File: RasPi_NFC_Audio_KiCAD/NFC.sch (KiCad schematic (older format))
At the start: 33 parts

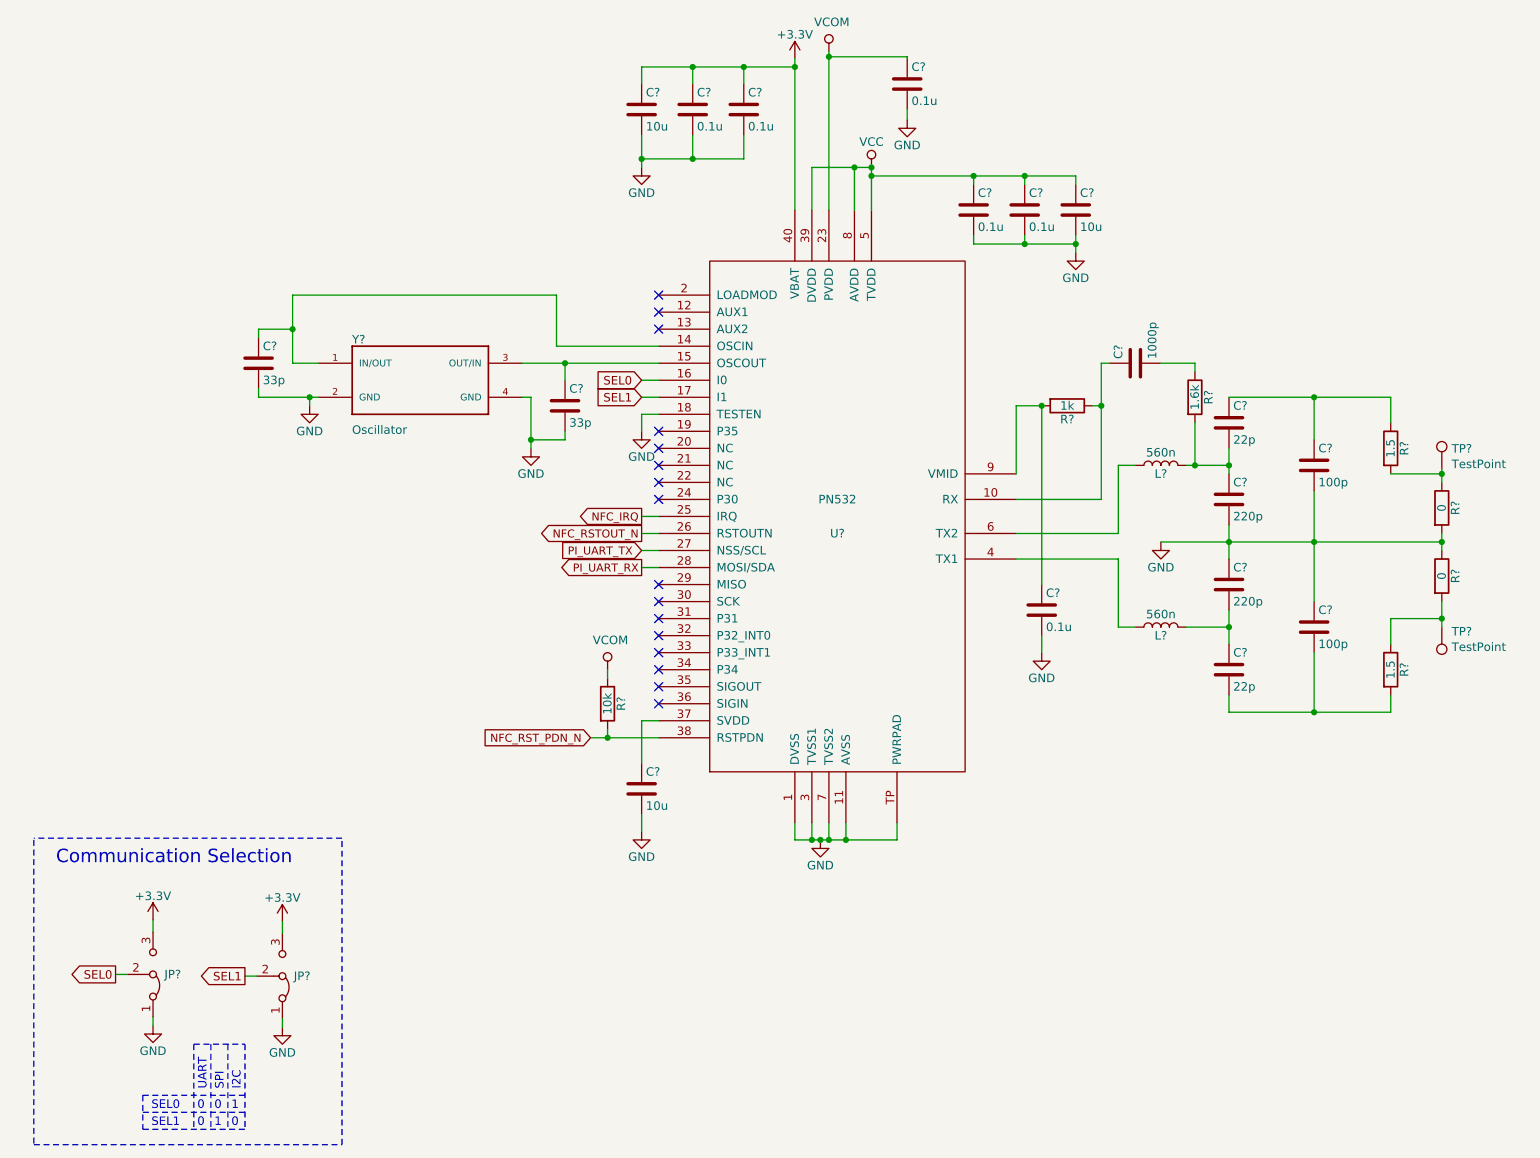
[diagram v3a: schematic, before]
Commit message: Schematic Updates
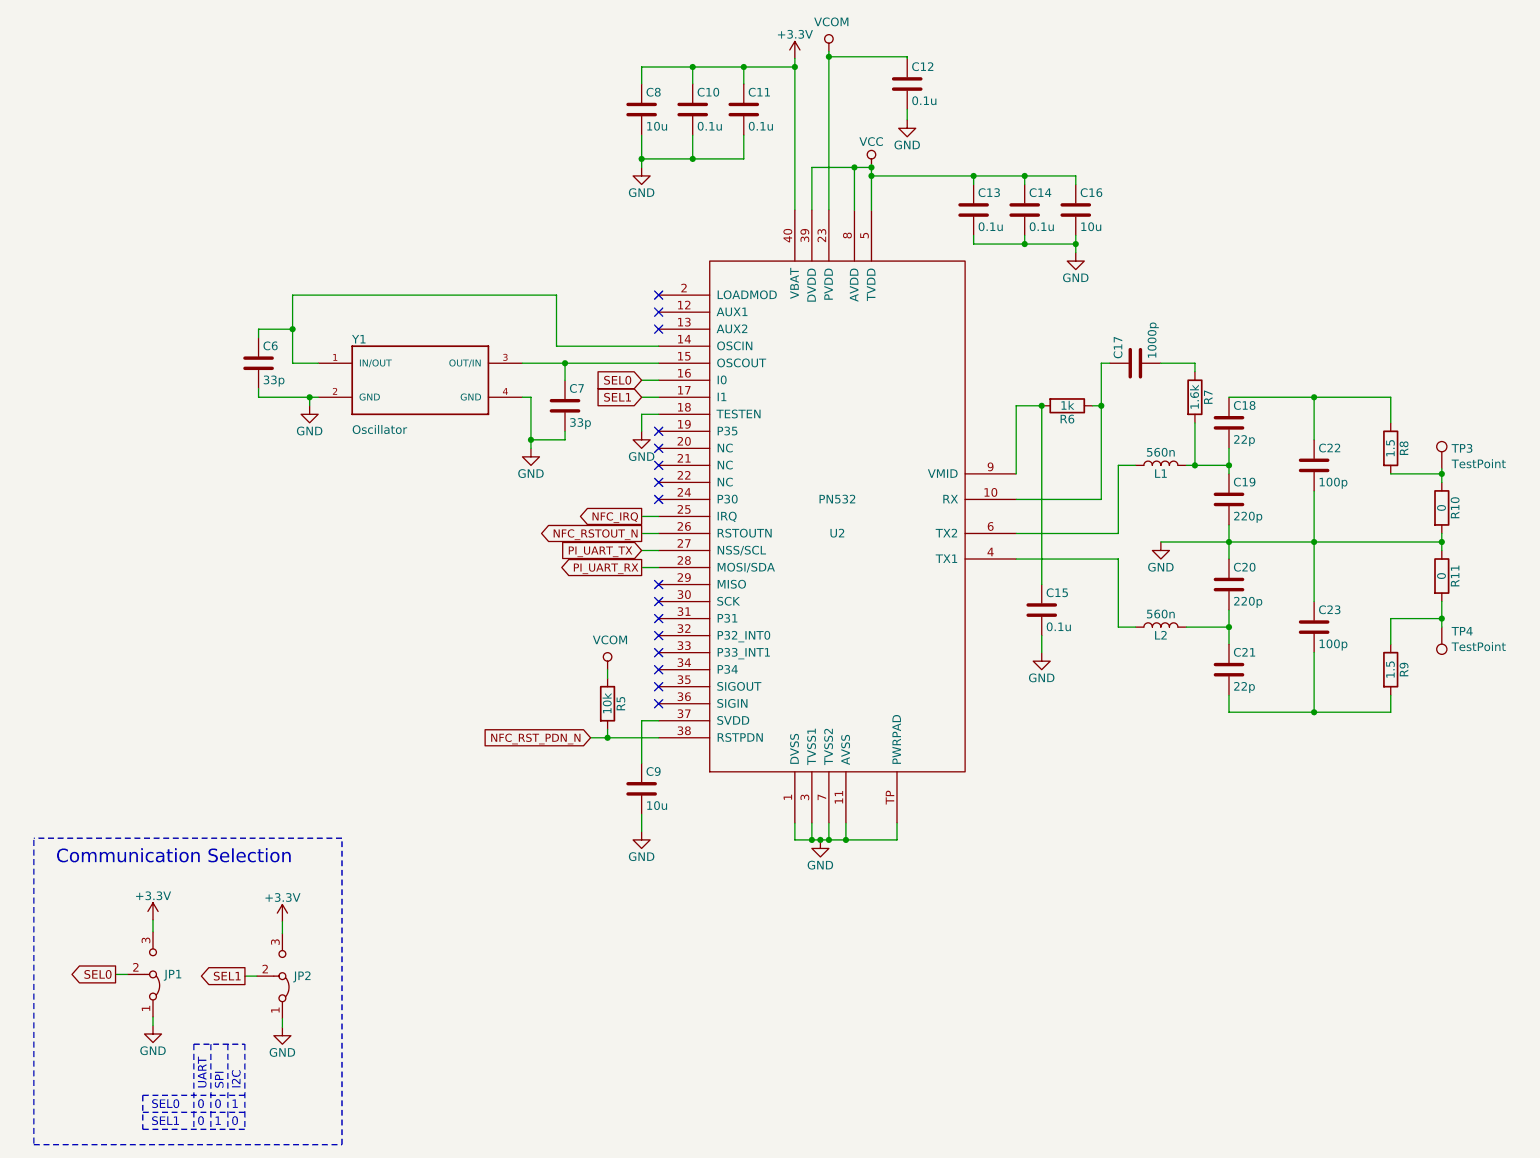
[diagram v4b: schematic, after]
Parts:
- gave numbers to parts that had none: 33
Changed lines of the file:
@@
 $EndDescr
 $Comp
-L PN532:PN532 U?
+L PN532:PN532 U2
 U 1 1 5ACE3C9F
 P 6400 3740
-F 0 "U?" H 6400 3640 50  0000 C CNN
+F 0 "U2" H 6400 3640 50  0000 C CNN
 F 1 "PN532" H 6400 3840 50  0000 C CNN
 F 2 "NFC_Toy_Lib:HVQFN40-6X6" H 6400 3740 50  0001 C CNN
@@
 	5250 4040 5350 4040
 $Comp
-L Oscillator:Oscillator Y?
+L Oscillator:Oscillator Y1
 U 1 1 5ACE46F9
 P 3950 2940
-F 0 "Y?" H 3549 3150 50  0000 L BNN
+F 0 "Y1" H 3549 3150 50  0000 L BNN
 F 1 "Oscillator" H 3549 2619 50  0000 L BNN
 F 2 "NFC_Toy_Lib:OSCCC500X320X105N" H 3950 2940 50  0001 L BNN
@@
 	6250 1690 6500 1690
 $Comp
-L Device:L L?
+L Device:L L1
 U 1 1 5ACEADE9
 P 8300 3440
-F 0 "L?" V 8250 3440 50  0000 C CNN
+F 0 "L1" V 8250 3440 50  0000 C CNN
 F 1 "560n" V 8375 3440 50  0000 C CNN
 F 2 "Inductors_SMD:L_0603_HandSoldering" H 8300 3440 50  0001 C CNN
@@
 $EndComp
 $Comp
-L Device:C C?
+L Device:C C19
 U 1 1 5ACEAE3A
 P 8700 3640
-F 0 "C?" H 8725 3740 50  0000 L CNN
+F 0 "C19" H 8725 3740 50  0000 L CNN
 F 1 "220p" H 8725 3540 50  0000 L CNN
 F 2 "Capacitors_SMD:C_0402" H 8738 3490 50  0001 C CNN
@@
 Connection ~ 6500 1690
 $Comp
-L Device:L L?
+L Device:L L2
 U 1 1 5ACEB747
 P 8300 4390
-F 0 "L?" V 8250 4390 50  0000 C CNN
+F 0 "L2" V 8250 4390 50  0000 C CNN
 F 1 "560n" V 8375 4390 50  0000 C CNN
 F 2 "Inductors_SMD:L_0603_HandSoldering" H 8300 4390 50  0001 C CNN
@@
 $EndComp
 $Comp
-L Device:C C?
+L Device:C C20
 U 1 1 5ACEB85B
 P 8700 4140
-F 0 "C?" H 8725 4240 50  0000 L CNN
+F 0 "C20" H 8725 4240 50  0000 L CNN
 F 1 "220p" H 8725 4040 50  0000 L CNN
 F 2 "Capacitors_SMD:C_0402" H 8738 3990 50  0001 C CNN
@@
 	8700 3340 8700 3440
 $Comp
-L Device:C C?
+L Device:C C18
 U 1 1 5ACEB929
 P 8700 3190
-F 0 "C?" H 8725 3290 50  0000 L CNN
+F 0 "C18" H 8725 3290 50  0000 L CNN
 F 1 "22p" H 8725 3090 50  0000 L CNN
 F 2 "Capacitors_SMD:C_0402" H 8738 3040 50  0001 C CNN
@@
 $EndComp
 $Comp
-L Device:C C?
+L Device:C C21
 U 1 1 5ACEB967
 P 8700 4640
-F 0 "C?" H 8725 4740 50  0000 L CNN
+F 0 "C21" H 8725 4740 50  0000 L CNN
 F 1 "22p" H 8725 4540 50  0000 L CNN
 F 2 "Capacitors_SMD:C_0402" H 8738 4490 50  0001 C CNN
@@
 $EndComp
 $Comp
-L Device:C C?
+L Device:C C23
 U 1 1 5ACEB9A1
 P 9200 4390
-F 0 "C?" H 9225 4490 50  0000 L CNN
+F 0 "C23" H 9225 4490 50  0000 L CNN
 F 1 "100p" H 9225 4290 50  0000 L CNN
 F 2 "Capacitors_SMD:C_0402" H 9238 4240 50  0001 C CNN
@@
 $EndComp
 $Comp
-L Device:C C?
+L Device:C C22
 U 1 1 5ACEB9F3
 P 9200 3440
-F 0 "C?" H 9225 3540 50  0000 L CNN
+F 0 "C22" H 9225 3540 50  0000 L CNN
 F 1 "100p" H 9225 3340 50  0000 L CNN
 F 2 "Capacitors_SMD:C_0402" H 9238 3290 50  0001 C CNN
@@
 Connection ~ 9200 3890
 $Comp
-L Device:R R?
+L Device:R R9
 U 1 1 5ACEBF6E
 P 9650 4640
-F 0 "R?" V 9730 4640 50  0000 C CNN
+F 0 "R9" V 9730 4640 50  0000 C CNN
 F 1 "1.5" V 9650 4640 50  0000 C CNN
 F 2 "Resistors_SMD:R_0603_HandSoldering" V 9580 4640 50  0001 C CNN
@@
 $EndComp
 $Comp
-L Device:R R?
+L Device:R R8
 U 1 1 5ACEBF75
 P 9650 3340
-F 0 "R?" V 9730 3340 50  0000 C CNN
+F 0 "R8" V 9730 3340 50  0000 C CNN
 F 1 "1.5" V 9650 3340 50  0000 C CNN
 F 2 "Resistors_SMD:R_0603_HandSoldering" V 9580 3340 50  0001 C CNN
@@
 Connection ~ 9200 3040
 $Comp
-L Device:R R?
+L Device:R R10
 U 1 1 5ACEC09A
 P 9950 3690
-F 0 "R?" V 10030 3690 50  0000 C CNN
+F 0 "R10" V 10030 3690 50  0000 C CNN
 F 1 "0" V 9950 3690 50  0000 C CNN
 F 2 "Resistors_SMD:R_0402" V 9880 3690 50  0001 C CNN
@@
 $EndComp
 $Comp
-L Device:R R?
+L Device:R R11
 U 1 1 5ACEC0EF
 P 9950 4090
-F 0 "R?" V 10030 4090 50  0000 C CNN
+F 0 "R11" V 10030 4090 50  0000 C CNN
 F 1 "0" V 9950 4090 50  0000 C CNN
 F 2 "Resistors_SMD:R_0402" V 9880 4090 50  0001 C CNN
@@
 	9950 4240 9950 4340
 $Comp
-L Device:R R?
+L Device:R R7
 U 1 1 5ACEC27D
 P 8500 3040
-F 0 "R?" V 8580 3040 50  0000 C CNN
+F 0 "R7" V 8580 3040 50  0000 C CNN
 F 1 "1.6k" V 8500 3040 50  0000 C CNN
 F 2 "Resistors_SMD:R_0603_HandSoldering" V 8430 3040 50  0001 C CNN
@@
 Connection ~ 8500 3440
 $Comp
-L Device:C C?
+L Device:C C17
 U 1 1 5ACEC388
 P 8150 2840
-F 0 "C?" H 8175 2940 50  0000 L CNN
+F 0 "C17" H 8175 2940 50  0000 L CNN
 F 1 "1000p" H 8175 2740 50  0000 L CNN
 F 2 "Capacitors_SMD:C_0402" H 8188 2690 50  0001 C CNN
@@
 	7950 3640 7450 3640
 $Comp
-L Device:R R?
+L Device:R R6
 U 1 1 5ACEC51A
 P 7750 3090
-F 0 "R?" V 7830 3090 50  0000 C CNN
+F 0 "R6" V 7830 3090 50  0000 C CNN
 F 1 "1k" V 7750 3090 50  0000 C CNN
 F 2 "Resistors_SMD:R_0603_HandSoldering" V 7680 3090 50  0001 C CNN
@@
 $EndComp
 $Comp
-L Device:C C?
+L Device:C C15
 U 1 1 5ACEC7D8
 P 7600 4290
-F 0 "C?" H 7625 4390 50  0000 L CNN
+F 0 "C15" H 7625 4390 50  0000 L CNN
 F 1 "0.1u" H 7625 4190 50  0000 L CNN
 F 2 "Capacitors_SMD:C_0402" H 7638 4140 50  0001 C CNN
@@
 	3000 3040 3300 3040
 $Comp
-L Device:C C?
+L Device:C C6
 U 1 1 5ACED3C6
 P 3000 2840
-F 0 "C?" H 3025 2940 50  0000 L CNN
+F 0 "C6" H 3025 2940 50  0000 L CNN
 F 1 "33p" H 3025 2740 50  0000 L CNN
 F 2 "Capacitors_SMD:C_0402" H 3038 2690 50  0001 C CNN
@@
 Connection ~ 3200 2640
 $Comp
-L Device:C C?
+L Device:C C7
 U 1 1 5ACED68A
 P 4800 3090
-F 0 "C?" H 4825 3190 50  0000 L CNN
+F 0 "C7" H 4825 3190 50  0000 L CNN
 F 1 "33p" H 4825 2990 50  0000 L CNN
 F 2 "Capacitors_SMD:C_0402" H 4838 2940 50  0001 C CNN
@@
 Connection ~ 6350 5640
 $Comp
-L Device:R R?
+L Device:R R5
 U 1 1 5ACEF2A4
 P 5050 4840
-F 0 "R?" V 5130 4840 50  0000 C CNN
+F 0 "R5" V 5130 4840 50  0000 C CNN
 F 1 "10k" V 5050 4840 50  0000 C CNN
 F 2 "Resistors_SMD:R_0603_HandSoldering" V 4980 4840 50  0001 C CNN
@@
 Connection ~ 5050 5040
 $Comp
-L Device:C C?
+L Device:C C13
 U 1 1 5ACEFF35
 P 7200 1940
-F 0 "C?" H 7225 2040 50  0000 L CNN
+F 0 "C13" H 7225 2040 50  0000 L CNN
 F 1 "0.1u" H 7225 1840 50  0000 L CNN
 F 2 "Capacitors_SMD:C_0402" H 7238 1790 50  0001 C CNN
@@
 $EndComp
 $Comp
-L Device:C C?
+L Device:C C14
 U 1 1 5ACEFFEF
 P 7500 1940
-F 0 "C?" H 7525 2040 50  0000 L CNN
+F 0 "C14" H 7525 2040 50  0000 L CNN
 F 1 "0.1u" H 7525 1840 50  0000 L CNN
 F 2 "Capacitors_SMD:C_0402" H 7538 1790 50  0001 C CNN
@@
 $EndComp
 $Comp
-L Device:C C?
+L Device:C C10
 U 1 1 5ACF004D
 P 5550 1350
-F 0 "C?" H 5575 1450 50  0000 L CNN
+F 0 "C10" H 5575 1450 50  0000 L CNN
 F 1 "0.1u" H 5575 1250 50  0000 L CNN
 F 2 "Capacitors_SMD:C_0402" H 5588 1200 50  0001 C CNN
@@
 $EndComp
 $Comp
-L Device:C C?
+L Device:C C11
 U 1 1 5ACF00B0
 P 5850 1350
-F 0 "C?" H 5875 1450 50  0000 L CNN
+F 0 "C11" H 5875 1450 50  0000 L CNN
 F 1 "0.1u" H 5875 1250 50  0000 L CNN
 F 2 "Capacitors_SMD:C_0402" H 5888 1200 50  0001 C CNN
@@
 	6600 1740 7200 1740
 $Comp
-L Device:C C?
+L Device:C C16
 U 1 1 5ACF059B
 P 7800 1940
-F 0 "C?" H 7825 2040 50  0000 L CNN
+F 0 "C16" H 7825 2040 50  0000 L CNN
 F 1 "10u" H 7825 1840 50  0000 L CNN
 F 2 "Capacitors_SMD:C_0603_HandSoldering" H 7838 1790 50  0001 C CNN
@@
 Connection ~ 5850 1100
 $Comp
-L Device:C C?
+L Device:C C8
 U 1 1 5ACF095C
 P 5250 1350
-F 0 "C?" H 5275 1450 50  0000 L CNN
+F 0 "C8" H 5275 1450 50  0000 L CNN
 F 1 "10u" H 5275 1250 50  0000 L CNN
 F 2 "Capacitors_SMD:C_0603_HandSoldering" H 5288 1200 50  0001 C CNN
@@
 Connection ~ 5550 1640
 $Comp
-L Device:C C?
+L Device:C C9
 U 1 1 5ACF126E
 P 5250 5340
-F 0 "C?" H 5275 5440 50  0000 L CNN
+F 0 "C9" H 5275 5440 50  0000 L CNN
 F 1 "10u" H 5275 5240 50  0000 L CNN
 F 2 "Capacitors_SMD:C_0603_HandSoldering" H 5288 5190 50  0001 C CNN
@@
 	6450 5640 6750 5640
 $Comp
-L Connector:TestPoint TP?
+L Connector:TestPoint TP3
 U 1 1 5E181FE8
 P 9950 3460
-F 0 "TP?" H 10008 3578 50  0000 L CNN
+F 0 "TP3" H 10008 3578 50  0000 L CNN
 F 1 "TestPoint" H 10008 3487 50  0000 L CNN
 F 2 "" H 10150 3460 50  0001 C CNN
@@
 $EndComp
 $Comp
-L Connector:TestPoint TP?
+L Connector:TestPoint TP4
 U 1 1 5E1839E2
 P 9950 4390
-F 0 "TP?" H 9892 4416 50  0000 R CNN
+F 0 "TP4" H 9892 4416 50  0000 R CNN
 F 1 "TestPoint" H 9892 4507 50  0000 R CNN
 F 2 "" H 10150 4390 50  0001 C CNN
@@
 $EndComp
 $Comp
-L Jumper:Jumper_3_Bridged12 JP?
+L Jumper:Jumper_3_Bridged12 JP1
 U 1 1 5E1BD36A
 P 2380 6430
-F 0 "JP?" V 2380 6497 50  0000 L CNN
+F 0 "JP1" V 2380 6497 50  0000 L CNN
 F 1 "Jumper_3_Bridged12" V 2335 6497 50  0001 L CNN
 F 2 "" H 2380 6430 50  0001 C CNN
@@
 $EndComp
 $Comp
-L Jumper:Jumper_3_Bridged12 JP?
+L Jumper:Jumper_3_Bridged12 JP2
 U 1 1 5E1D4093
 P 3140 6440
-F 0 "JP?" V 3140 6507 50  0000 L CNN
+F 0 "JP2" V 3140 6507 50  0000 L CNN
 F 1 "Jumper_3_Bridged12" V 3095 6507 50  0001 L CNN
 F 2 "" H 3140 6440 50  0001 C CNN
@@
 	6350 1010 6350 1040
 $Comp
-L Device:C C?
+L Device:C C12
 U 1 1 5E208532
 P 6810 1200
-F 0 "C?" H 6835 1300 50  0000 L CNN
+F 0 "C12" H 6835 1300 50  0000 L CNN
 F 1 "0.1u" H 6835 1100 50  0000 L CNN
 F 2 "Capacitors_SMD:C_0402" H 6848 1050 50  0001 C CNN

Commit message: Schematic updates
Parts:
- C10, C11, C12, C13, C14, C15: DigiKey (none) -> 1276-1000-1-ND; Part # (none) -> CL10B104KB8NNNC
- C6, C7: DigiKey (none) -> 399-7896-1-ND; Part # (none) -> C0603C330J1GACTU
- R5: DigiKey (none) -> RNCP0603FTD10K0CT-ND; Part # (none) -> RNCP0603FTD10K0
- U2: DigiKey (none) -> 568-13228-ND; Part # (none) -> PN5321A3HN/C106,55
- Y1: DigiKey (none) -> 887-1424-1-ND; Part # (none) -> 7M-27.120MAAJ-T
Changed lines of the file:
@@
 F 2 "NFC_Toy_Lib:HVQFN40-6X6" H 6400 3740 50  0001 C CNN
 F 3 "DOCUMENTATION" H 6400 3740 50  0001 C CNN
+F 4 "PN5321A3HN/C106,55" H 6400 3740 50  0001 C CNN "Part #"
+F 5 "568-13228-ND" H 6400 3740 50  0001 C CNN "DigiKey"
 	1    6400 3740
 	1    0    0    -1
@@
 F 7 "Oscillator" H 3950 2940 50  0001 L BNN "Field7"
 F 8 "Good" H 3950 2940 50  0001 L BNN "Field8"
+F 9 "7M-27.120MAAJ-T" H 3950 2940 50  0001 C CNN "Part #"
+F 10 "887-1424-1-ND" H 3950 2940 50  0001 C CNN "DigiKey"
 	1    3950 2940
 	1    0    0    -1
@@
 F 2 "Capacitors_SMD:C_0402" H 7638 4140 50  0001 C CNN
 F 3 "" H 7600 4290 50  0001 C CNN
+F 4 "CL10B104KB8NNNC" H 7600 4290 50  0001 C CNN "Part #"
+F 5 "1276-1000-1-ND" H 7600 4290 50  0001 C CNN "DigiKey"
 	1    7600 4290
 	1    0    0    -1
@@
 F 2 "Capacitors_SMD:C_0402" H 3038 2690 50  0001 C CNN
 F 3 "" H 3000 2840 50  0001 C CNN
+F 4 "C0603C330J1GACTU" H 3000 2840 50  0001 C CNN "Part #"
+F 5 "399-7896-1-ND" H 3000 2840 50  0001 C CNN "DigiKey"
 	1    3000 2840
 	1    0    0    -1
@@
 F 2 "Capacitors_SMD:C_0402" H 4838 2940 50  0001 C CNN
 F 3 "" H 4800 3090 50  0001 C CNN
+F 4 "C0603C330J1GACTU" H 4800 3090 50  0001 C CNN "Part #"
+F 5 "399-7896-1-ND" H 4800 3090 50  0001 C CNN "DigiKey"
 	1    4800 3090
 	1    0    0    -1
@@
 F 2 "Resistors_SMD:R_0603_HandSoldering" V 4980 4840 50  0001 C CNN
 F 3 "" H 5050 4840 50  0001 C CNN
+F 4 "RNCP0603FTD10K0" H 5050 4840 50  0001 C CNN "Part #"
+F 5 "RNCP0603FTD10K0CT-ND" H 5050 4840 50  0001 C CNN "DigiKey"
 	1    5050 4840
 	1    0    0    -1
@@
 F 2 "Capacitors_SMD:C_0402" H 7238 1790 50  0001 C CNN
 F 3 "" H 7200 1940 50  0001 C CNN
+F 4 "CL10B104KB8NNNC" H 7200 1940 50  0001 C CNN "Part #"
+F 5 "1276-1000-1-ND" H 7200 1940 50  0001 C CNN "DigiKey"
 	1    7200 1940
 	1    0    0    -1
@@
 F 2 "Capacitors_SMD:C_0402" H 7538 1790 50  0001 C CNN
 F 3 "" H 7500 1940 50  0001 C CNN
+F 4 "CL10B104KB8NNNC" H 7500 1940 50  0001 C CNN "Part #"
+F 5 "1276-1000-1-ND" H 7500 1940 50  0001 C CNN "DigiKey"
 	1    7500 1940
 	1    0    0    -1
@@
 F 2 "Capacitors_SMD:C_0402" H 5588 1200 50  0001 C CNN
 F 3 "" H 5550 1350 50  0001 C CNN
+F 4 "CL10B104KB8NNNC" H 5550 1350 50  0001 C CNN "Part #"
+F 5 "1276-1000-1-ND" H 5550 1350 50  0001 C CNN "DigiKey"
 	1    5550 1350
 	1    0    0    -1
@@
 F 2 "Capacitors_SMD:C_0402" H 5888 1200 50  0001 C CNN
 F 3 "" H 5850 1350 50  0001 C CNN
+F 4 "CL10B104KB8NNNC" H 5850 1350 50  0001 C CNN "Part #"
+F 5 "1276-1000-1-ND" H 5850 1350 50  0001 C CNN "DigiKey"
 	1    5850 1350
 	1    0    0    -1
@@
 F 2 "Capacitors_SMD:C_0402" H 6848 1050 50  0001 C CNN
 F 3 "" H 6810 1200 50  0001 C CNN
+F 4 "CL10B104KB8NNNC" H 6810 1200 50  0001 C CNN "Part #"
+F 5 "1276-1000-1-ND" H 6810 1200 50  0001 C CNN "DigiKey"
 	1    6810 1200
 	1    0    0    -1

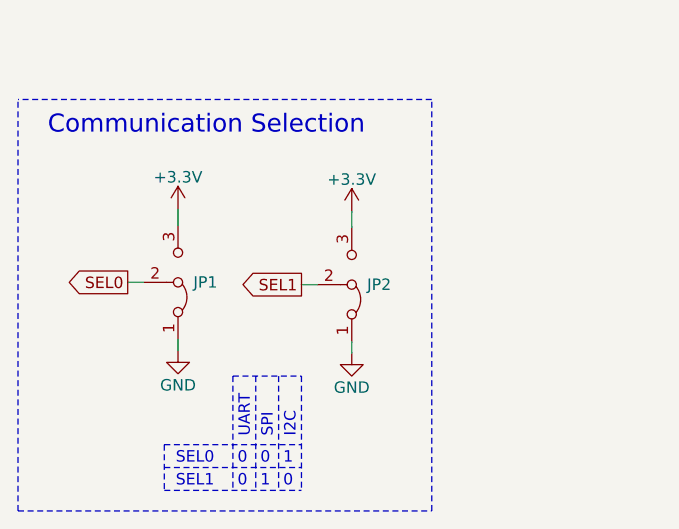
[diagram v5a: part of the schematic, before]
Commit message: Schematic changes
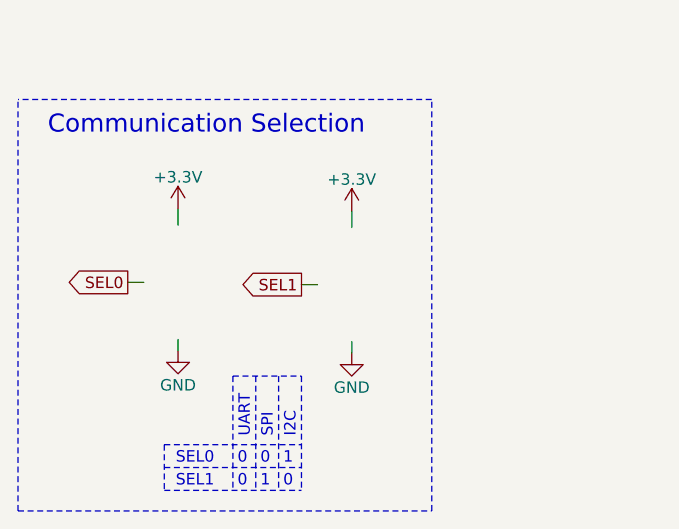
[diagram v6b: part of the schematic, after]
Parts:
- removed JP1, JP2: Jumper_3_Bridged12, symbol Jumper:Jumper_3_Bridged12
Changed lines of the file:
@@
 	1    0    0    -1
-$EndComp
-$Comp
-L Jumper:Jumper_3_Bridged12 JP1
-U 1 1 5E1BD36A
-P 2380 6430
-F 0 "JP1" V 2380 6497 50  0000 L CNN
-F 1 "Jumper_3_Bridged12" V 2335 6497 50  0001 L CNN
-F 2 "" H 2380 6430 50  0001 C CNN
-F 3 "~" H 2380 6430 50  0001 C CNN
-	1    2380 6430
-	0    1    -1   0
 $EndComp
 Wire Wire Line
@@
 	1    0    0    -1
 $EndComp
-$Comp
-L Jumper:Jumper_3_Bridged12 JP2
-U 1 1 5E1D4093
-P 3140 6440
-F 0 "JP2" V 3140 6507 50  0000 L CNN
-F 1 "Jumper_3_Bridged12" V 3095 6507 50  0001 L CNN
-F 2 "" H 3140 6440 50  0001 C CNN
-F 3 "~" H 3140 6440 50  0001 C CNN
-	1    3140 6440
-	0    1    -1   0
-$EndComp
 Wire Wire Line
